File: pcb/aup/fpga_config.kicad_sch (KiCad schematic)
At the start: 1 part, among them U1 XC7A50T-FGG484

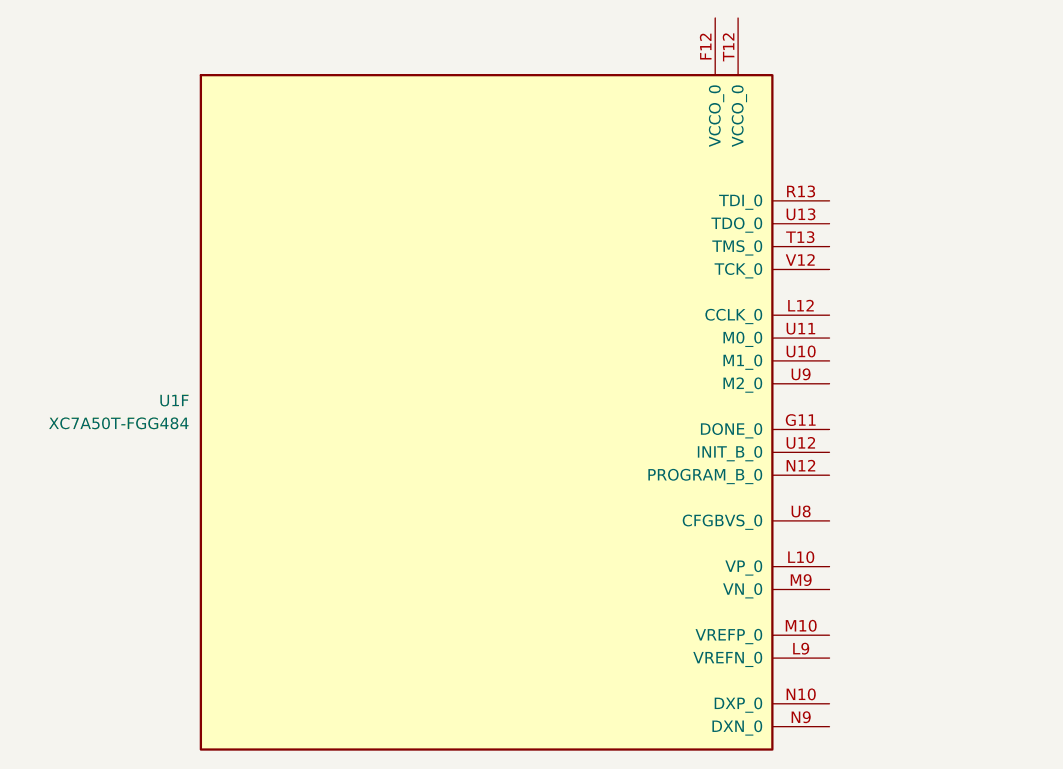
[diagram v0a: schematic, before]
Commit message: Relative path fixes
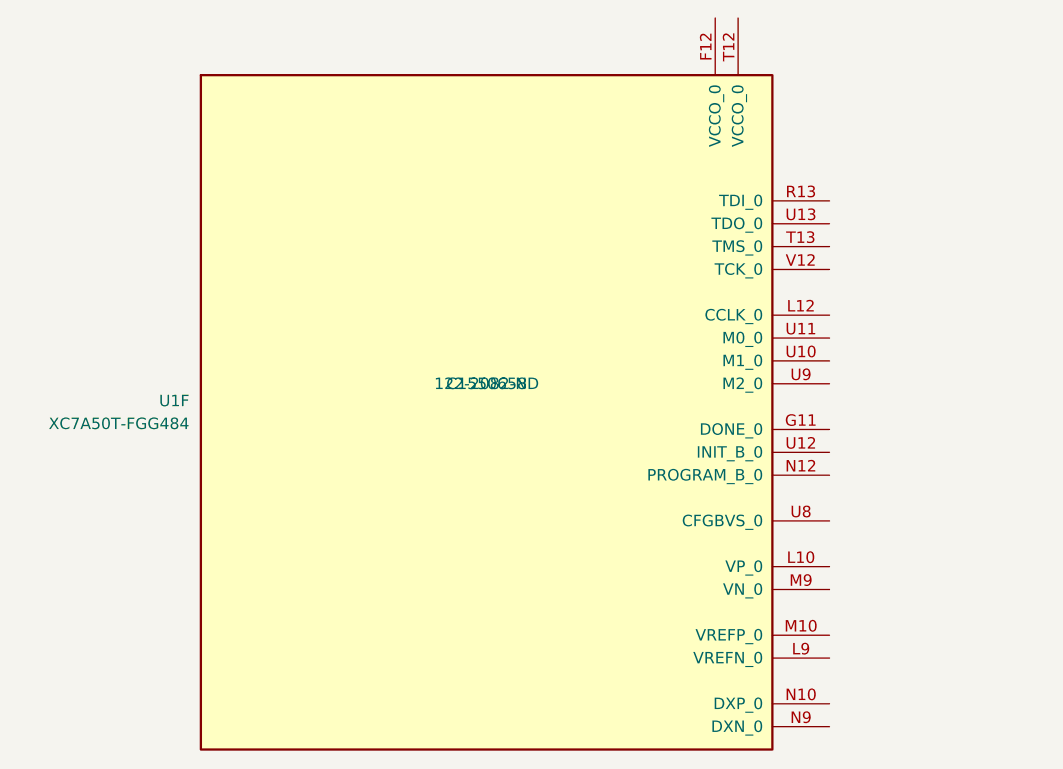
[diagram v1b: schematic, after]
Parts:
- U1: footprint Package_BGA:Xilinx_FGG484 -> !Xilinx:Xilinx_FGG484; Digi-Key Part Number (none) -> 122-2082-ND; LCSC Part # (none) -> C1550658
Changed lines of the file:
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@@
 			)
 		)
-		(property "Footprint" "Package_BGA:Xilinx_FGG484"
+		(property "Footprint" "!Xilinx:Xilinx_FGG484"
 			(at 71.12 63.5 0)
 			(effects
@@
 			)
 		)
-		(property "Description" "Artix 7 T 50 XC7A50T-FGG484"
+		(property "Description" "XC7A50T-2FGG484C"
 			(at 71.12 63.5 0)
 			(effects
@@
 			)
 		)
+		(property "LCSC Part #" "C1550658"
+			(at 71.12 63.5 0)
+			(effects
+				(font
+					(size 1.27 1.27)
+				)
+			)
+		)
+		(property "Digi-Key Part Number" "122-2082-ND"
+			(at 71.12 63.5 0)
+			(effects
+				(font
+					(size 1.27 1.27)
+				)
+			)
+		)

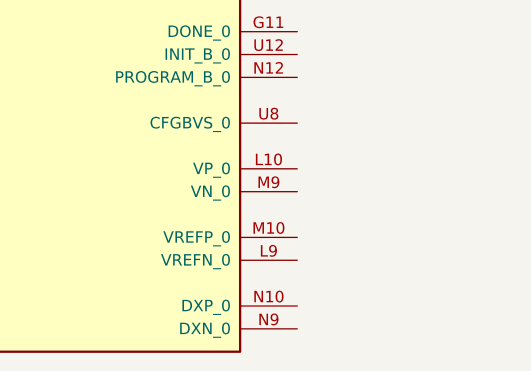
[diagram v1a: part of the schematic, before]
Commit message: Add netnames for rails
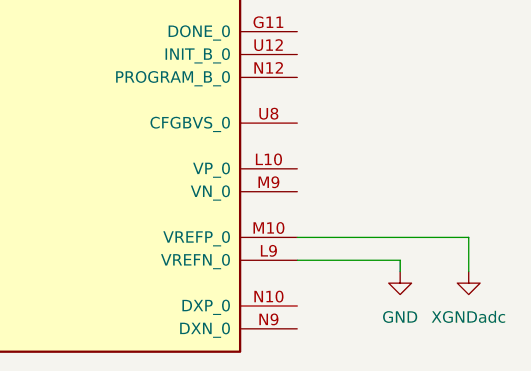
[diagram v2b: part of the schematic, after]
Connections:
- net GND: now reaches U1.L9 (VREFN_0)
- net XGNDadc: now reaches U1.M10 (VREFP_0)
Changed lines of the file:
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@@
 	(generator_version "9.0")
 	(paper "A4")
+	(wire
+		(pts
+			(xy 109.22 91.44) (xy 128.27 91.44)
+		)
+		(stroke
+			(width 0)
+			(type default)
+		)
+	)
+	(wire
+		(pts
+			(xy 128.27 95.25) (xy 128.27 91.44)
+		)
+		(stroke
+			(width 0)
+			(type default)
+		)
+	)
+	(wire
+		(pts
+			(xy 120.65 93.98) (xy 120.65 95.25)
+		)
+		(stroke
+			(width 0)
+			(type default)
+		)
+	)
+	(wire
+		(pts
+			(xy 109.22 93.98) (xy 120.65 93.98)
+		)
+		(stroke
+			(width 0)
+			(type default)
+		)
+	)
 	(symbol
 		(lib_id "!Xilinx:XC7A50T-FGG484")
@@
 				)
 			)
+		)
+	)
+	(symbol
+		(lib_id "power:GND")
+		(at 128.27 95.25 0)
+		(unit 1)
+		(exclude_from_sim no)
+		(in_bom yes)
+		(on_board yes)
+		(dnp no)
+		(fields_autoplaced yes)
+		(property "Reference" "#PWR032"
+			(at 128.27 101.6 0)
+			(effects
+				(font
+					(size 1.27 1.27)
+				)
+				(hide yes)
+			)
+		)
+		(property "Value" "XGNDadc"
+			(at 128.27 100.33 0)
+			(effects
+				(font
+					(size 1.27 1.27)
+				)
+			)
+		)
+		(property "Footprint" ""
+			(at 128.27 95.25 0)
+			(effects
+				(font
+					(size 1.27 1.27)
+				)
+				(hide yes)
+			)
+		)
+		(property "Datasheet" ""
+			(at 128.27 95.25 0)
+			(effects
+				(font
+					(size 1.27 1.27)
+				)
+				(hide yes)
+			)
+		)
+		(property "Description" "Power symbol creates a global label with name \"GND\" , ground"
+			(at 128.27 95.25 0)
+			(effects
+				(font
+					(size 1.27 1.27)
+				)
+				(hide yes)
+			)
+		)
+		(pin "1"
+		)
+		(instances
+			(project "aup"
+				(path "/312a869c-f247-4883-8e23-bdad51e1754f/f3030c28-a39b-499d-a242-1a3634e8e6f9"
+					(reference "#PWR032")
+					(unit 1)
+				)
+			)
+		)
+	)
+	(symbol
+		(lib_id "power:GND")
+		(at 120.65 95.25 0)
+		(unit 1)
+		(exclude_from_sim no)
+		(in_bom yes)
+		(on_board yes)
+		(dnp no)
+		(fields_autoplaced yes)
+		(property "Reference" "#PWR035"
+			(at 120.65 101.6 0)
+			(effects
+				(font
+					(size 1.27 1.27)
+				)
+				(hide yes)
+			)
+		)
+		(property "Value" "GND"
+			(at 120.65 100.33 0)
+			(effects
+				(font
+					(size 1.27 1.27)
+				)
+			)
+		)
+		(property "Footprint" ""
+			(at 120.65 95.25 0)
+			(effects
+				(font
+					(size 1.27 1.27)
+				)
+				(hide yes)
+			)
+		)
+		(property "Datasheet" ""
+			(at 120.65 95.25 0)
+			(effects
+				(font
+					(size 1.27 1.27)
+				)
+				(hide yes)
+			)
+		)
+		(property "Description" "Power symbol creates a global label with name \"GND\" , ground"
+			(at 120.65 95.25 0)
+			(effects
+				(font
+					(size 1.27 1.27)
+				)
+				(hide yes)
+			)
+		)
+		(pin "1"
+		)
+		(instances
+			(project ""
+				(path "/312a869c-f247-4883-8e23-bdad51e1754f/f3030c28-a39b-499d-a242-1a3634e8e6f9"
+					(reference "#PWR035")
+					(unit 1)
+				)
+			)
